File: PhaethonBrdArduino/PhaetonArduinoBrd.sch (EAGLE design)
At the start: 40 parts, among them IC1 DS1307, IC2 LM2596T, Q1 32.768 Hz, SW1 EC12E_SW

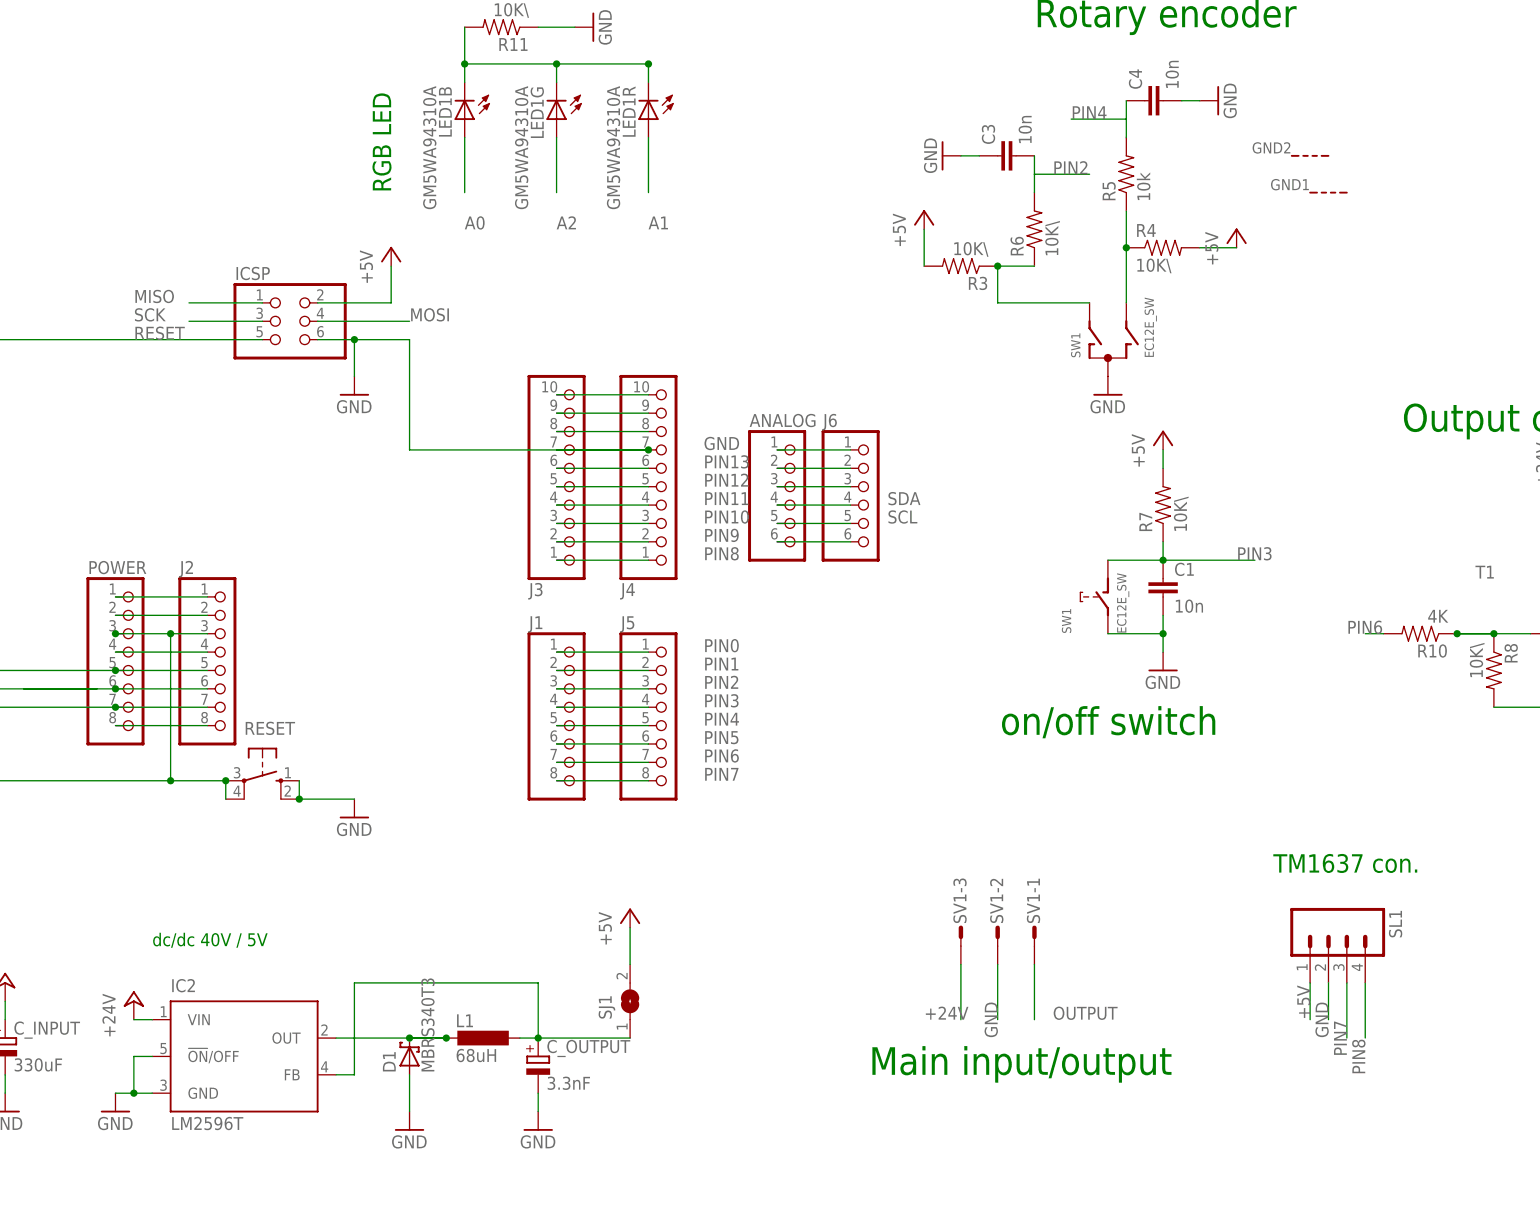
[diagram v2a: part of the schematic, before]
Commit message: Updated schematic and first board is designed
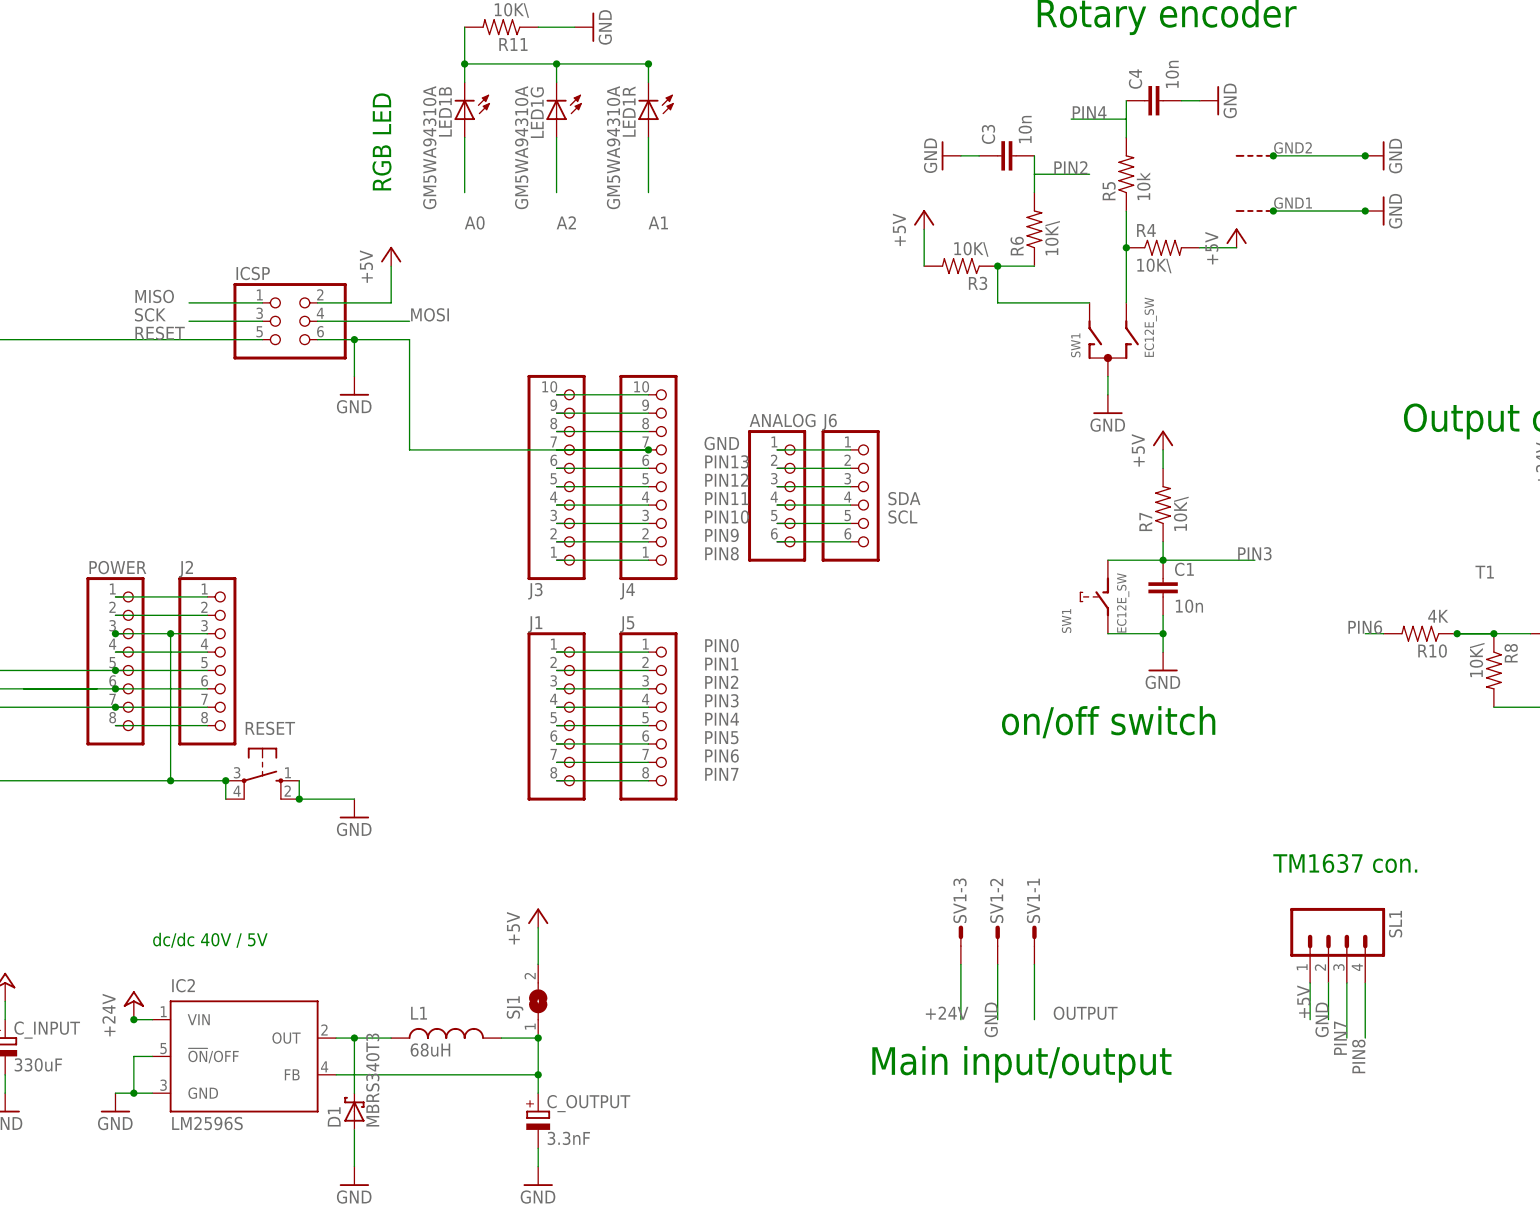
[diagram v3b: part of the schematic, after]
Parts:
- IC2: value LM2596T -> LM2596S; device national-semiconductor:LM2596T -> national-semiconductor:LM2596S
- L1: device rcl:L-EUL5038P -> inductor-coilcraft:MSS1260
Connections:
- removed net N$1: D1.C, IC2.OUT, L1.2
- removed net N$10: C_OUTPUT.+, IC2.FB, L1.1, SJ1.1
- new net OUTPUT1: D1.C, IC2.OUT, L1.P$2
- new net OUTPUT5V: C_OUTPUT.+, IC2.FB, L1.P$1, SJ1.1
- net GND: now also SW1G$3.G, SW1G$4.G
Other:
- moved on the sheet: C_OUTPUT, D1, SJ1
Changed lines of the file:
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@@
 <part name="R9" library="SparkFun" deviceset="RESISTOR" device="" value="20K"/>
 <part name="R10" library="SparkFun" deviceset="RESISTOR" device="" value="4K"/>
-<part name="IC2" library="national-semiconductor" deviceset="LM2596" device="T"/>
+<part name="IC2" library="national-semiconductor" deviceset="LM2596" device="S" value="LM2596S"/>
 <part name="GND13" library="supply1" deviceset="GND" device=""/>
 <part name="SJ1" library="jumper" deviceset="SJ" device=""/>
 <part name="P+11" library="supply1" deviceset="+5V" device=""/>
 <part name="P+12" library="supply1" deviceset="+24V" device=""/>
-<part name="L1" library="rcl" deviceset="L-EU" device="L5038P" value="68uH"/>
 <part name="D1" library="diode" deviceset="MBRS3*0T3" device="" technology="4"/>
 <part name="C_OUTPUT" library="resistor" deviceset="CPOL-EU" device="140CLH-1010" value="3.3nF"/>
@@
 <part name="GND17" library="supply1" deviceset="GND" device=""/>
 <part name="SL1" library="con-amp-quick" deviceset="M04" device=""/>
+<part name="L1" library="inductor-coilcraft" deviceset="MSS1260" device="" value="68uH"/>
+<part name="GND18" library="supply1" deviceset="GND" device=""/>
+<part name="GND19" library="supply1" deviceset="GND" device=""/>
 </parts>
 <sheets>
@@
 <instance part="SW1" gate="G$1" x="165.1" y="66.04"/>
 <instance part="SW1" gate="G$2" x="165.1" y="33.02" rot="R90"/>
-<instance part="SW1" gate="G$3" x="193.04" y="88.9"/>
-<instance part="SW1" gate="G$4" x="190.5" y="93.98"/>
-<instance part="GND6" gate="1" x="165.1" y="60.96"/>
+<instance part="SW1" gate="G$3" x="187.96" y="86.36" rot="R180"/>
+<instance part="SW1" gate="G$4" x="187.96" y="93.98" rot="R180"/>
+<instance part="GND6" gate="1" x="165.1" y="58.42"/>
 <instance part="P+6" gate="1" x="139.7" y="86.36"/>
 <instance part="P+7" gate="1" x="182.88" y="83.82"/>
@@
 <instance part="IC2" gate="G$1" x="45.72" y="-30.48"/>
 <instance part="GND13" gate="1" x="27.94" y="-38.1"/>
-<instance part="SJ1" gate="1" x="99.06" y="-22.86" rot="R90"/>
-<instance part="P+11" gate="1" x="99.06" y="-10.16"/>
+<instance part="SJ1" gate="1" x="86.36" y="-22.86" rot="R90"/>
+<instance part="P+11" gate="1" x="86.36" y="-10.16"/>
 <instance part="P+12" gate="1" x="30.48" y="-22.86"/>
-<instance part="L1" gate="G$1" x="78.74" y="-27.94" rot="R270"/>
-<instance part="D1" gate="G$1" x="68.58" y="-30.48" rot="R90"/>
-<instance part="C_OUTPUT" gate="G$1" x="86.36" y="-30.48"/>
+<instance part="D1" gate="G$1" x="60.96" y="-38.1" rot="R90"/>
+<instance part="C_OUTPUT" gate="G$1" x="86.36" y="-38.1"/>
 <instance part="C_INPUT" gate="G$1" x="12.7" y="-27.94"/>
 <instance part="P+13" gate="1" x="12.7" y="-20.32"/>
 <instance part="GND14" gate="1" x="12.7" y="-38.1"/>
-<instance part="GND15" gate="1" x="86.36" y="-40.64"/>
-<instance part="GND16" gate="1" x="68.58" y="-40.64"/>
+<instance part="GND15" gate="1" x="86.36" y="-48.26"/>
+<instance part="GND16" gate="1" x="60.96" y="-48.26"/>
 <instance part="SV1" gate="-1" x="154.94" y="-12.7" rot="R270"/>
 <instance part="SV1" gate="-2" x="149.86" y="-12.7" rot="R270"/>
@@
 <instance part="GND17" gate="1" x="93.98" y="111.76" rot="R90"/>
 <instance part="SL1" gate="G$1" x="195.58" y="-15.24" rot="R270"/>
+<instance part="L1" gate="G$1" x="73.66" y="-27.94" rot="R270"/>
+<instance part="GND18" gate="1" x="203.2" y="93.98" rot="R90"/>
+<instance part="GND19" gate="1" x="203.2" y="86.36" rot="R90"/>
 </instances>
 <busses>
@@
 <segment>
 <pinref part="SJ1" gate="1" pin="2"/>
-<wire x1="99.06" y1="-17.78" x2="99.06" y2="-12.7" width="0.1524" layer="91"/>
+<wire x1="86.36" y1="-17.78" x2="86.36" y2="-12.7" width="0.1524" layer="91"/>
 <pinref part="P+11" gate="1" pin="+5V"/>
 </segment>
@@
 <pinref part="SW1" gate="G$1" pin="C"/>
 <pinref part="GND6" gate="1" pin="GND"/>
+<wire x1="165.1" y1="60.96" x2="165.1" y2="63.5" width="0.1524" layer="91"/>
 </segment>
 <segment>
@@
 <pinref part="C_OUTPUT" gate="G$1" pin="-"/>
 <pinref part="GND15" gate="1" pin="GND"/>
-<wire x1="86.36" y1="-38.1" x2="86.36" y2="-35.56" width="0.1524" layer="91"/>
+<wire x1="86.36" y1="-45.72" x2="86.36" y2="-43.18" width="0.1524" layer="91"/>
 </segment>
 <segment>
 <pinref part="D1" gate="G$1" pin="A"/>
 <pinref part="GND16" gate="1" pin="GND"/>
-<wire x1="68.58" y1="-38.1" x2="68.58" y2="-33.02" width="0.1524" layer="91"/>
+<wire x1="60.96" y1="-45.72" x2="60.96" y2="-40.64" width="0.1524" layer="91"/>
 </segment>
 <segment>
@@
 <wire x1="195.58" y1="-20.32" x2="195.58" y2="-25.4" width="0.1524" layer="91"/>
 <label x="195.58" y="-27.94" size="1.778" layer="95" rot="R90"/>
+</segment>
+<segment>
+<pinref part="GND19" gate="1" pin="GND"/>
+<wire x1="187.96" y1="86.36" x2="200.66" y2="86.36" width="0.1524" layer="91"/>
+<pinref part="SW1" gate="G$3" pin="G"/>
+<junction x="187.96" y="86.36"/>
+<junction x="200.66" y="86.36"/>
+</segment>
+<segment>
+<pinref part="GND18" gate="1" pin="GND"/>
+<wire x1="200.66" y1="93.98" x2="187.96" y2="93.98" width="0.1524" layer="91"/>
+<pinref part="SW1" gate="G$4" pin="G"/>
+<junction x="187.96" y="93.98"/>
+<junction x="200.66" y="93.98"/>
 </segment>
 </net>
@@
 <pinref part="P+12" gate="1" pin="+24V"/>
 <wire x1="30.48" y1="-25.4" x2="33.02" y2="-25.4" width="0.1524" layer="91"/>
+<junction x="30.48" y="-25.4"/>
 </segment>
 <segment>
@@
 <pinref part="J5" gate="A" pin="7"/>
 <label x="109.22" y="10.16" size="1.778" layer="95"/>
-</segment>
-</net>
-<net name="N$1" class="0">
-<segment>
-<pinref part="IC2" gate="G$1" pin="OUT"/>
-<wire x1="58.42" y1="-27.94" x2="68.58" y2="-27.94" width="0.1524" layer="91"/>
-<pinref part="D1" gate="G$1" pin="C"/>
-<pinref part="L1" gate="G$1" pin="2"/>
-<junction x="73.66" y="-27.94"/>
-<wire x1="68.58" y1="-27.94" x2="73.66" y2="-27.94" width="0.1524" layer="91"/>
-<wire x1="73.66" y1="-27.94" x2="68.58" y2="-27.94" width="0.1524" layer="91"/>
-<junction x="68.58" y="-27.94"/>
-</segment>
-</net>
-<net name="N$10" class="0">
-<segment>
-<pinref part="SJ1" gate="1" pin="1"/>
-<pinref part="L1" gate="G$1" pin="1"/>
-<wire x1="99.06" y1="-27.94" x2="86.36" y2="-27.94" width="0.1524" layer="91"/>
-<pinref part="C_OUTPUT" gate="G$1" pin="+"/>
-<wire x1="86.36" y1="-27.94" x2="83.82" y2="-27.94" width="0.1524" layer="91"/>
-<junction x="86.36" y="-27.94"/>
-<pinref part="IC2" gate="G$1" pin="FB"/>
-<wire x1="58.42" y1="-33.02" x2="60.96" y2="-33.02" width="0.1524" layer="91"/>
-<wire x1="60.96" y1="-33.02" x2="60.96" y2="-20.32" width="0.1524" layer="91"/>
-<wire x1="60.96" y1="-20.32" x2="86.36" y2="-20.32" width="0.1524" layer="91"/>
-<wire x1="86.36" y1="-20.32" x2="86.36" y2="-27.94" width="0.1524" layer="91"/>
 </segment>
 </net>
@@
 </segment>
 </net>
+<net name="OUTPUT1" class="0">
+<segment>
+<pinref part="IC2" gate="G$1" pin="OUT"/>
+<wire x1="66.04" y1="-27.94" x2="60.96" y2="-27.94" width="0.1524" layer="91"/>
+<pinref part="D1" gate="G$1" pin="C"/>
+<wire x1="60.96" y1="-27.94" x2="58.42" y2="-27.94" width="0.1524" layer="91"/>
+<wire x1="60.96" y1="-35.56" x2="60.96" y2="-27.94" width="0.1524" layer="91"/>
+<junction x="60.96" y="-27.94"/>
+<pinref part="L1" gate="G$1" pin="P$2"/>
+</segment>
+</net>
+<net name="OUTPUT5V" class="0">
+<segment>
+<pinref part="C_OUTPUT" gate="G$1" pin="+"/>
+<wire x1="81.28" y1="-27.94" x2="86.36" y2="-27.94" width="0.1524" layer="91"/>
+<wire x1="86.36" y1="-27.94" x2="86.36" y2="-33.02" width="0.1524" layer="91"/>
+<pinref part="IC2" gate="G$1" pin="FB"/>
+<wire x1="86.36" y1="-33.02" x2="86.36" y2="-35.56" width="0.1524" layer="91"/>
+<wire x1="58.42" y1="-33.02" x2="86.36" y2="-33.02" width="0.1524" layer="91"/>
+<pinref part="SJ1" gate="1" pin="1"/>
+<junction x="86.36" y="-27.94"/>
+<junction x="86.36" y="-33.02"/>
+<pinref part="L1" gate="G$1" pin="P$1"/>
+</segment>
+</net>

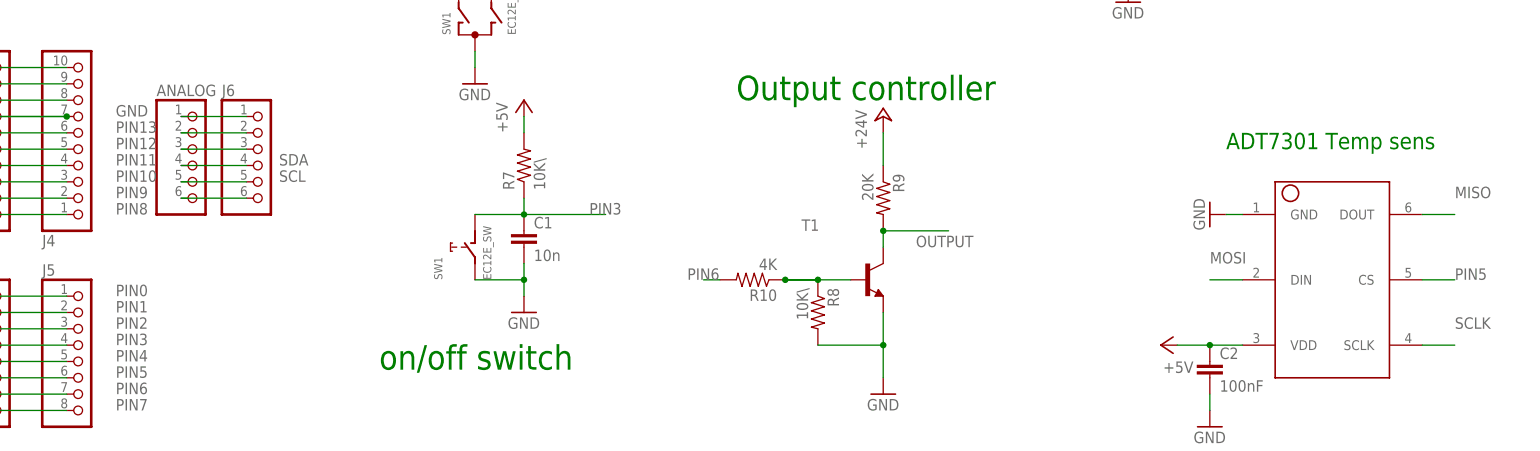
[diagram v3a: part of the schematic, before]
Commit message: Bug fixed, Temperature sens was not connected
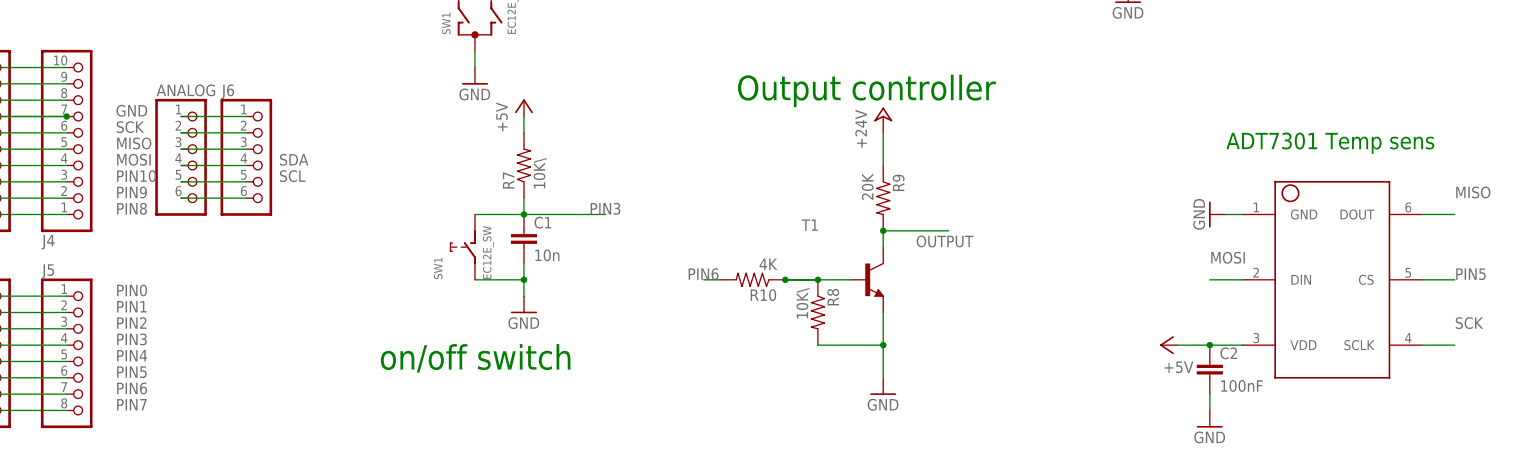
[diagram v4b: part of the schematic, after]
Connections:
- removed net PIN11: J3.4, J4.4
- removed net PIN12: J3.5, J4.5
- removed net PIN13: J3.6, J4.6
- removed net SCLK: U$2.SCLK
- net MISO: now also J3.5, J4.5
- net MOSI: now also J3.4, J4.4
- net SCK: now also J3.6, J4.6, U$2.SCLK
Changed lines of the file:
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@@
-</segment>
-</net>
-<net name="PIN12" class="0">
-<segment>
-<wire x1="101.6" y1="48.26" x2="88.9" y2="48.26" width="0.1524" layer="91"/>
-<pinref part="J3" gate="A" pin="5"/>
-<pinref part="J4" gate="A" pin="5"/>
-<label x="109.22" y="48.26" size="1.778" layer="95"/>
 </segment>
 </net>
@@
 </segment>
 </net>
-<net name="PIN11" class="0">
+<net name="MOSI" class="0">
+<segment>
+<pinref part="ICSP" gate="A" pin="4"/>
+<wire x1="55.88" y1="71.12" x2="68.58" y2="71.12" width="0.1524" layer="91"/>
+<label x="68.58" y="71.12" size="1.778" layer="95"/>
+</segment>
+<segment>
+<pinref part="U$2" gate="G$1" pin="DIN"/>
+<wire x1="284.48" y1="27.94" x2="279.4" y2="27.94" width="0.1524" layer="91"/>
+<label x="279.4" y="30.48" size="1.778" layer="95"/>
+</segment>
 <segment>
 <pinref part="J4" gate="A" pin="4"/>
@@
 </segment>
 </net>
-<net name="MOSI" class="0">
-<segment>
-<pinref part="ICSP" gate="A" pin="4"/>
-<wire x1="55.88" y1="71.12" x2="68.58" y2="71.12" width="0.1524" layer="91"/>
-<label x="68.58" y="71.12" size="1.778" layer="95"/>
-</segment>
-<segment>
-<pinref part="U$2" gate="G$1" pin="DIN"/>
-<wire x1="284.48" y1="27.94" x2="279.4" y2="27.94" width="0.1524" layer="91"/>
-<label x="279.4" y="30.48" size="1.778" layer="95"/>
-</segment>
-</net>
 <net name="SCK" class="0">
 <segment>
@@
 <label x="30.48" y="71.12" size="1.778" layer="95"/>
 </segment>
+<segment>
+<pinref part="U$2" gate="G$1" pin="SCLK"/>
+<wire x1="312.42" y1="17.78" x2="317.5" y2="17.78" width="0.1524" layer="91"/>
+<label x="317.5" y="20.32" size="1.778" layer="95"/>
+</segment>
+<segment>
+<pinref part="J4" gate="A" pin="6"/>
+<wire x1="101.6" y1="50.8" x2="88.9" y2="50.8" width="0.1524" layer="91"/>
+<pinref part="J3" gate="A" pin="6"/>
+<label x="109.22" y="50.8" size="1.778" layer="95"/>
+</segment>
 </net>
 <net name="MISO" class="0">
@@
 <wire x1="312.42" y1="38.1" x2="317.5" y2="38.1" width="0.1524" layer="91"/>
 <label x="317.5" y="40.64" size="1.778" layer="95"/>
+</segment>
+<segment>
+<wire x1="101.6" y1="48.26" x2="88.9" y2="48.26" width="0.1524" layer="91"/>
+<pinref part="J3" gate="A" pin="5"/>
+<pinref part="J4" gate="A" pin="5"/>
+<label x="109.22" y="48.26" size="1.778" layer="95"/>
 </segment>
 </net>
@@
 <pinref part="J5" gate="A" pin="5"/>
 <label x="109.22" y="15.24" size="1.778" layer="95"/>
-</segment>
-</net>
-<net name="SCLK" class="0">
-<segment>
-<pinref part="U$2" gate="G$1" pin="SCLK"/>
-<wire x1="312.42" y1="17.78" x2="317.5" y2="17.78" width="0.1524" layer="91"/>
-<label x="317.5" y="20.32" size="1.778" layer="95"/>
 </segment>
 </net>
@@
 </segment>
 </net>
-<net name="PIN13" class="0">
-<segment>
-<pinref part="J4" gate="A" pin="6"/>
-<wire x1="101.6" y1="50.8" x2="88.9" y2="50.8" width="0.1524" layer="91"/>
-<pinref part="J3" gate="A" pin="6"/>
-<label x="109.22" y="50.8" size="1.778" layer="95"/>
-</segment>
-</net>

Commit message: a lot of bug fixes
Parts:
- renumbered IC1 to DS1307, LED1 to LED, SL1 to DISPLAYCONNECTOR, U$2 to ADT
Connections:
- removed net N$141: J3.9, J4.9
- removed net N$142: J3.10, J4.10
- removed net N$23: ANALOG.6, J6.6
- new net A3: ANALOG.4, J6.4
- net OUTPUT1: now also L1.P$1; no longer L1.P$2
- net OUTPUT5V: now also L1.P$2; no longer L1.P$1
- net SCL: now also ANALOG.6, J3.10, J4.10, J6.6; no longer ANALOG.5, J6.5
- net SDA: now also ANALOG.5, J3.9, J4.9, J6.5; no longer ANALOG.4, J6.4
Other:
- moved on the sheet: L1
